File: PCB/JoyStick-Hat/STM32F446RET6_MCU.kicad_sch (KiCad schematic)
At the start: 40 parts, among them J12 BU2032SM-JJ-GTR, J13 20021121-00010C4LF, J14 0675031020, SW1 TL3301NF260QG, U5 STM32F446VETx, X1 ABM3B-8.000MHZ-B2-T, X2 ABS07-32.768KHZ-9-T

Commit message: PCB Created
Schematic and footprint bugs knocked out PCB created and parts imported into board.
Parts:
- C1, C11, C12, C14, C3: footprint growbox-KiCAD-Capacitors:C0402 -> AVR-KiCAD-Lib-Capacitors:C0402
- J12: footprint AVR-KiCAD-Lib-Connectors:BU2032SM-JJ-GTR -> AVR-KiCAD-Lib-Battery-Holders:BU2032SM-JJ-GTR
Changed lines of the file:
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@@
       (effects (font (size 1.27 1.27)) hide)
     )
-    (property "Footprint" "growbox-KiCAD-Capacitors:C0402" (at 137.16 190.5 0)
+    (property "Footprint" "AVR-KiCAD-Lib-Capacitors:C0402" (at 137.16 190.5 0)
       (effects (font (size 1.27 1.27)) hide)
     )
@@
       (effects (font (size 1.27 1.27)) hide)
     )
-    (property "Footprint" "growbox-KiCAD-Capacitors:C0402" (at 19.05 63.5 0)
+    (property "Footprint" "AVR-KiCAD-Lib-Capacitors:C0402" (at 13.97 62.23 0)
       (effects (font (size 1.27 1.27)) hide)
     )
@@
       (effects (font (size 1.27 1.27)) hide)
     )
-    (property "Footprint" "growbox-KiCAD-Capacitors:C0402" (at 39.37 63.5 0)
+    (property "Footprint" "AVR-KiCAD-Lib-Capacitors:C0402" (at 39.37 63.5 0)
       (effects (font (size 1.27 1.27)) hide)
     )
@@
       (effects (font (size 1.27 1.27)) hide)
     )
-    (property "Footprint" "growbox-KiCAD-Capacitors:C0402" (at 152.4 190.5 0)
+    (property "Footprint" "AVR-KiCAD-Lib-Capacitors:C0402" (at 152.4 190.5 0)
       (effects (font (size 1.27 1.27)) hide)
     )
@@
       (effects (font (size 1.27 1.27)) hide)
     )
-    (property "Footprint" "growbox-KiCAD-Capacitors:C0402" (at 25.4 154.94 0)
+    (property "Footprint" "AVR-KiCAD-Lib-Capacitors:C0402" (at 25.4 154.94 0)
       (effects (font (size 1.27 1.27)) hide)
     )
@@
       (effects (font (size 1.27 1.27)))
     )
-    (property "Footprint" "AVR-KiCAD-Lib-Connectors:BU2032SM-JJ-GTR" (at 77.47 16.51 0)
-      (effects (font (size 1.27 1.27)) hide)
-    )
+    (property "Footprint" "AVR-KiCAD-Lib-Battery-Holders:BU2032SM-JJ-GTR" (at 77.47 16.51 0)
+      (effects (font (size 1.27 1.27)) hide)
+    )

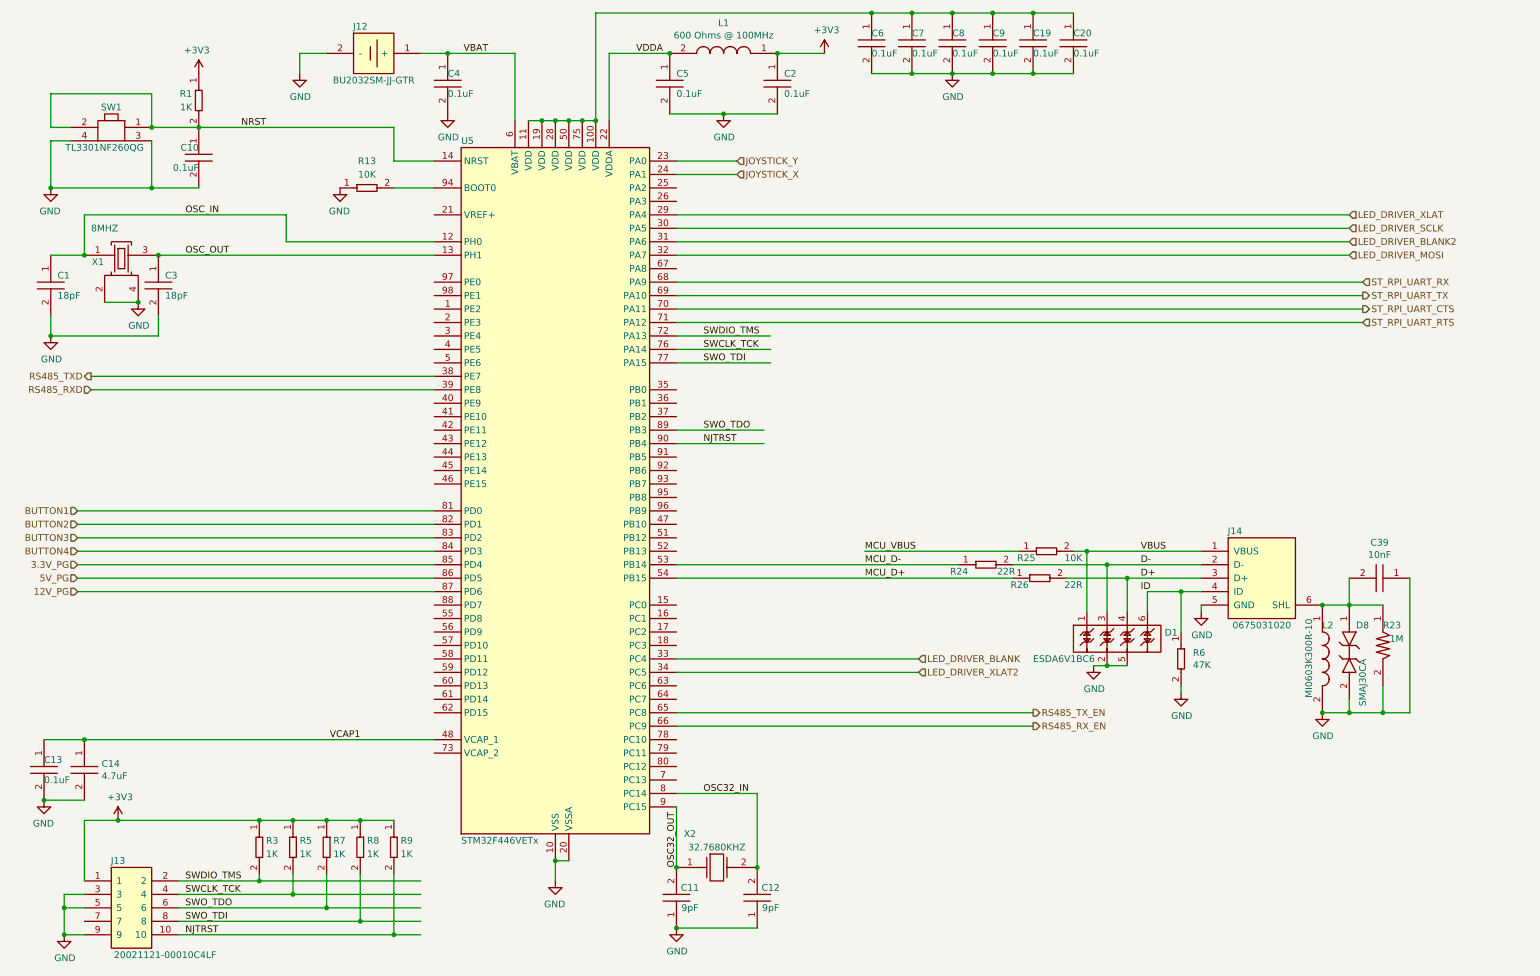
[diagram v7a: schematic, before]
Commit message: LEDs and Additional connectors
Added heartbeat and diagnostic LEDs to STM32 and RPi3 schematics so we can directly flash them for debug purposes. Added a connector for serial port diagnostics on STM32. Added rotary switch interface for STM32 and added pullups to button connectors.
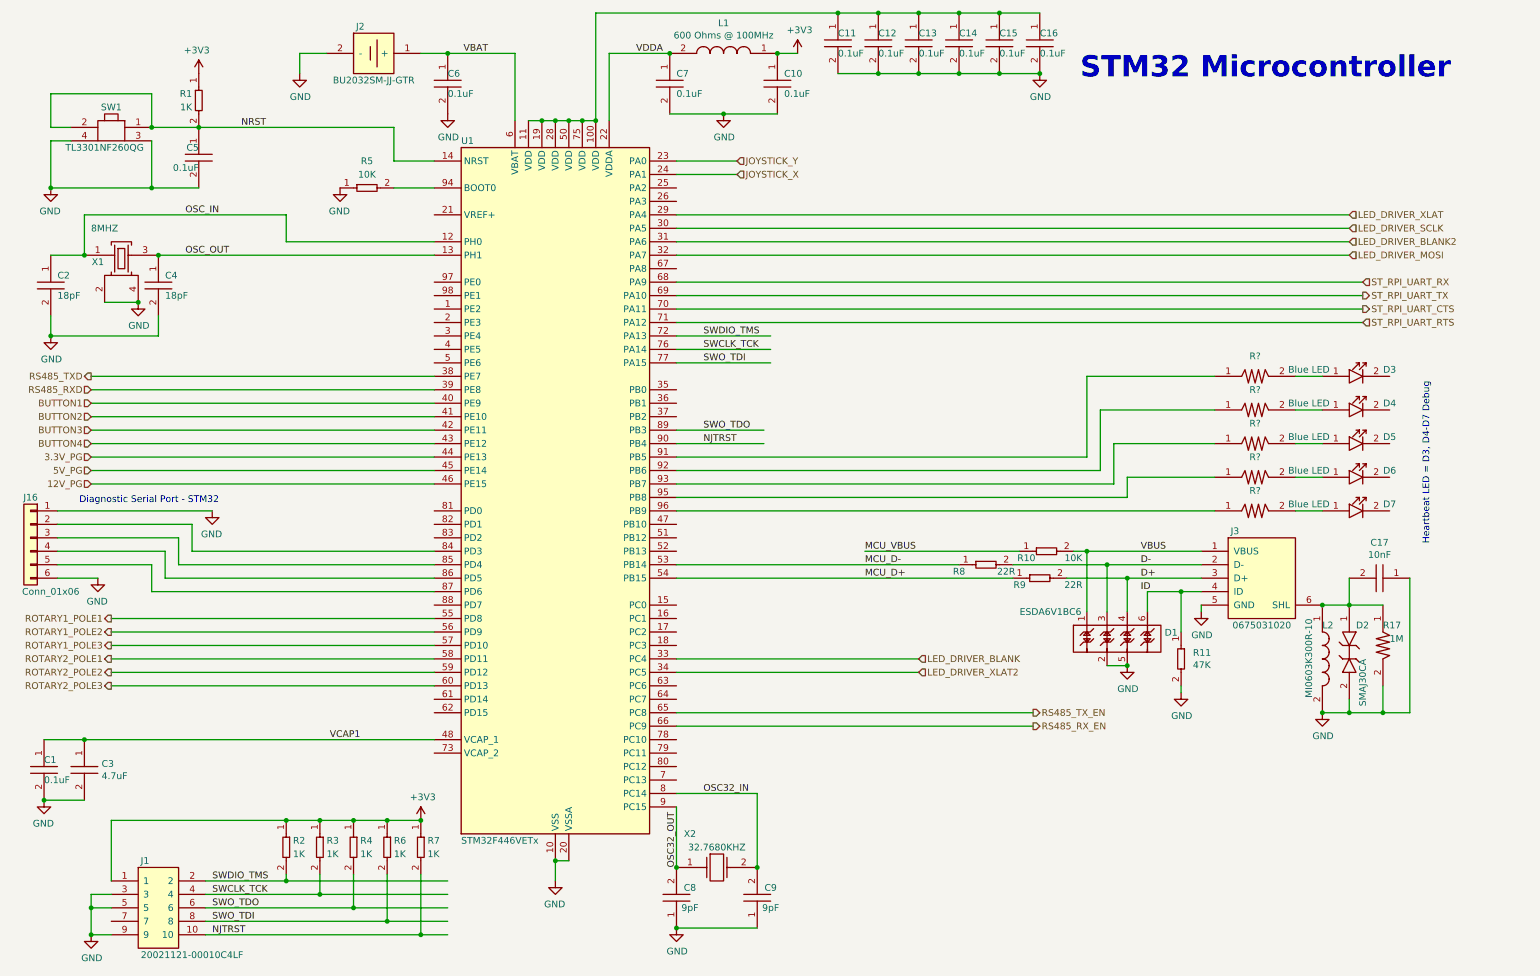
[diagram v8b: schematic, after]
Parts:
- added D3, D4, D5, D6, D7: LTST-C194TBKT, AVR-KiCAD-Lib-Diodes:LED0603, symbol AVR-KiCAD-Lib-Diodes:LTST-C194TBKT
- added J16: Conn_01x06, Connector_PinHeader_2.54mm:PinHeader_1x06_P2.54mm_Vertical, symbol Connector_Generic:Conn_01x06
- added R? (x5): RC0603FR-07470RL, AVR-KiCAD-Lib-Resistors:R0603, symbol AVR-KiCAD-Lib-Resistors:RC0603FR-07470RL
- renumbered C13 to C1, C2 to C10, C6 to C11, C7 to C12, C8 to C13, C9 to C14, C19 to C15, C20 to C16, C39 to C17, C1 to C2, C14 to C3, C3 to C4, C10 to C5, C4 to C6, C5 to C7, C11 to C8, C12 to C9, D8 to D2, J13 to J1, J12 to J2, J14 to J3, R25 to R10, R6 to R11, R23 to R17, R3 to R2, R5 to R3, R7 to R4, R13 to R5, R8 to R6, R9 to R7, R24 to R8, R26 to R9, U5 to U1
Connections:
- net 12V_PG: now also U1.46 (PE15); no longer U1.87 (PD6)
- net 3.3V_PG: now also U1.44 (PE13); no longer U1.85 (PD4)
- net 5V_PG: now also U1.45 (PE14); no longer U1.86 (PD5)
- net BUTTON1: now also U1.40 (PE9); no longer U1.81 (PD0)
- net BUTTON2: now also U1.41 (PE10); no longer U1.82 (PD1)
- net BUTTON3: now also U1.42 (PE11); no longer U1.83 (PD2)
- net BUTTON4: now also U1.43 (PE12); no longer U1.84 (PD3)
- net GND: now also J16.1 (Pin_1), J16.6 (Pin_6)
- net ROTARY1_POLE1: now reaches U1.55 (PD8)
- net ROTARY1_POLE2: now reaches U1.56 (PD9)
- net ROTARY1_POLE3: now reaches U1.57 (PD10)
- net ROTARY2_POLE1: now reaches U1.58 (PD11)
- net ROTARY2_POLE2: now reaches U1.59 (PD12)
- net ROTARY2_POLE3: now reaches U1.60 (PD13)
- net at U1.91 (PB5): now also R?.1
- net at U1.92 (PB6): now also R?.1
- net at U1.93 (PB7): now also R?.1
- net at U1.95 (PB8): now also R?.1
- net at U1.96 (PB9): now also R?.1
- new net: D3.1, R?.2
- new net: D7.1, R?.2
- new net: D5.1, R?.2
- new net: D6.1, R?.2
- new net: J16.2 (Pin_2), U1.84 (PD3)
- new net: J16.3 (Pin_3), U1.85 (PD4)
- new net: J16.4 (Pin_4), U1.86 (PD5)
- new net: J16.5 (Pin_5), U1.87 (PD6)
- new net: D4.1, R?.2
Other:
- note added: "Diagnostic Serial Port - STM32"
- note added: "Heartbeat LED = D3, D4-D7 Debug"
- note added: "STM32 Microcontroller"
- moved on the sheet: C11, C12, C13, C14, C15, C16, J1, R2, R3, R4, R6, R7
